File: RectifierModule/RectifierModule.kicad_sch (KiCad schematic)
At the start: 18 parts, among them J1 TransformerIn, J2 Rectified Out, J3 AuxIn, J4 VA, J5 Extra, J5 FAN, P1 Conn_WallPlug, U1 LM7812_TO220

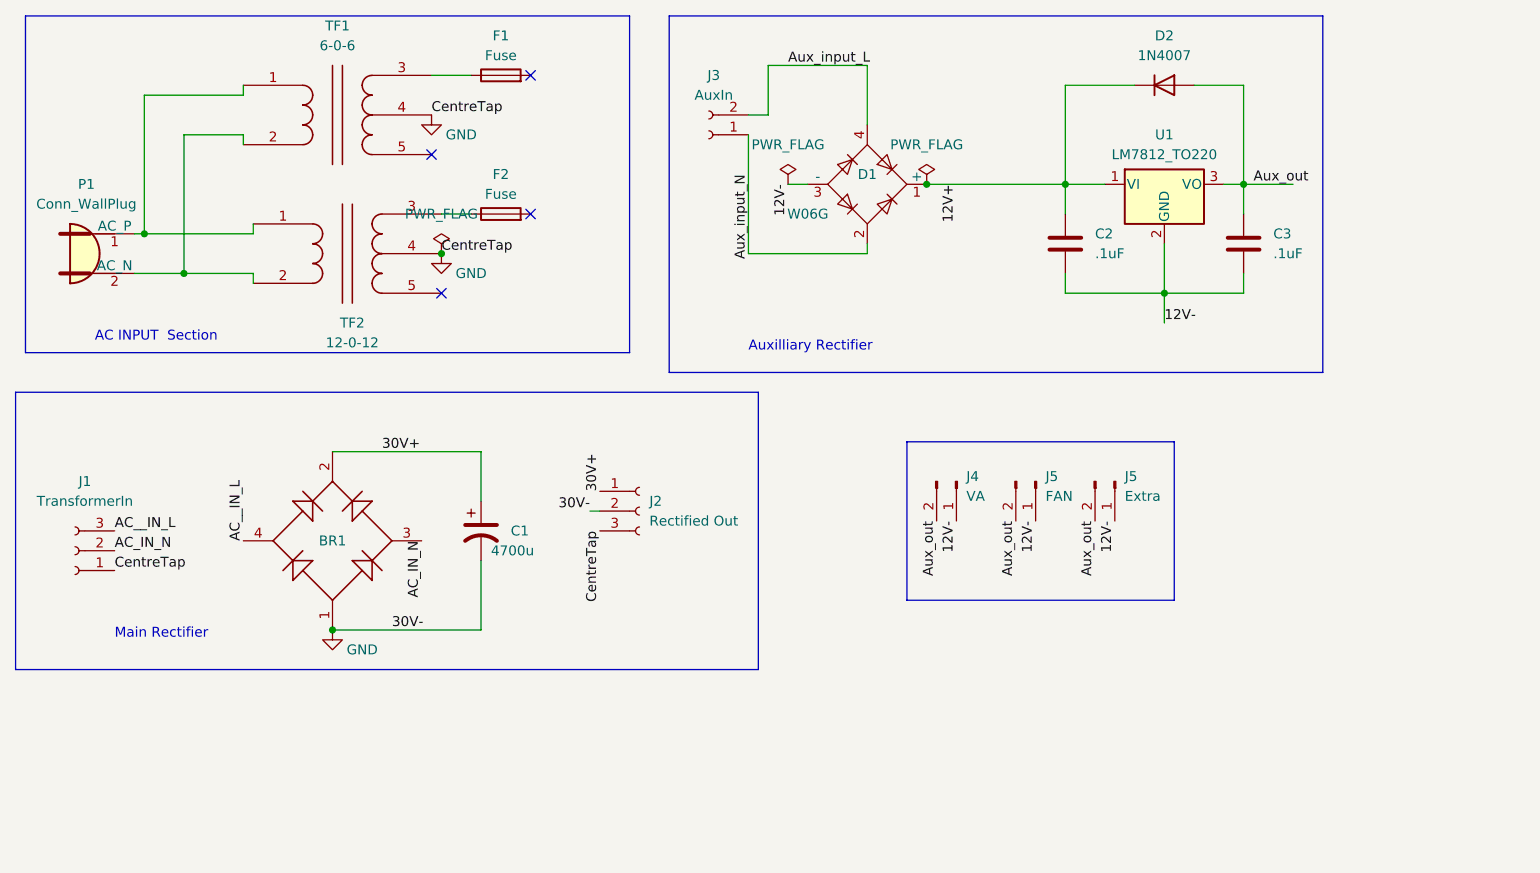
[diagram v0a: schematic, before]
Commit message: Updated net lists in the schematic
The schematic has all nets assigned to a net class. And the schematic has been tidied up
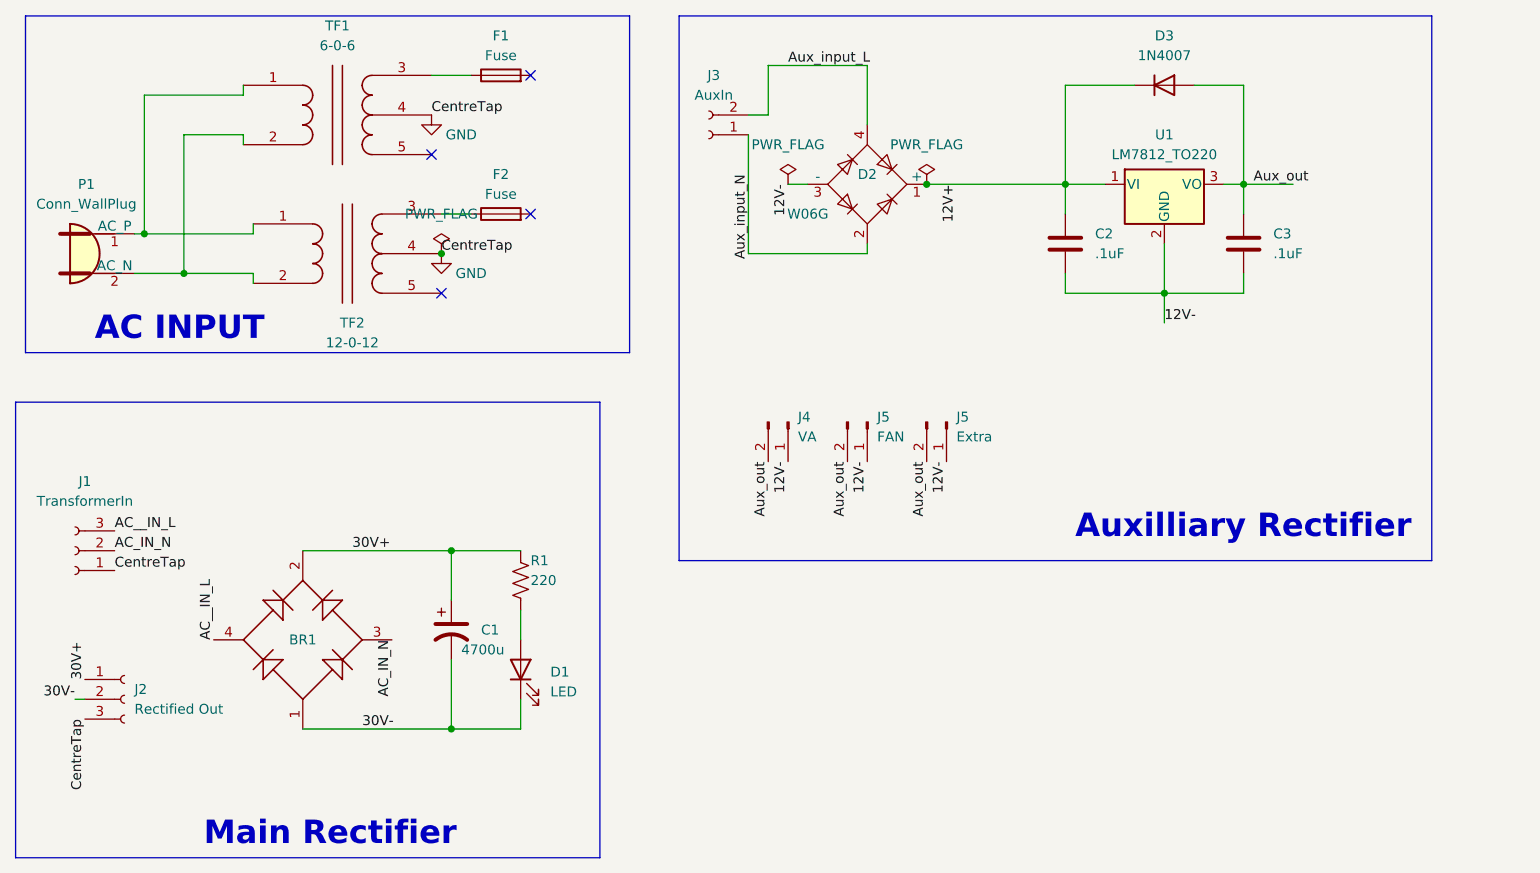
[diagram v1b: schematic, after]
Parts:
- added D1: LED, symbol Device:LED
- added R1: 220, symbol Device:R_US
- renumbered D1 to D2, D2 to D3
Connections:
- net 30V+: now also R1.1
- net GND: no longer BR1.1, C1.2, J2.2 (Pin_2)
- new net: D1.2 (A), R1.2
- new net 30V-: BR1.1, C1.2, D1.1 (K), J2.2 (Pin_2)
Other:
- note added: "AC INPUT"
- note removed: "AC INPUT Section"
- moved on the sheet: BR1, C1, J2, J4, J5

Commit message: Fixed all ERC warnings
There were several ERC warning regarding mismatch in port types. These have been fixed by modifying the library symbols
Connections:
- net AC__IN_L renamed AC_IN_L
- net GND renamed CentreTap
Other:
- moved on the sheet: F1, F2, TF1, TF2

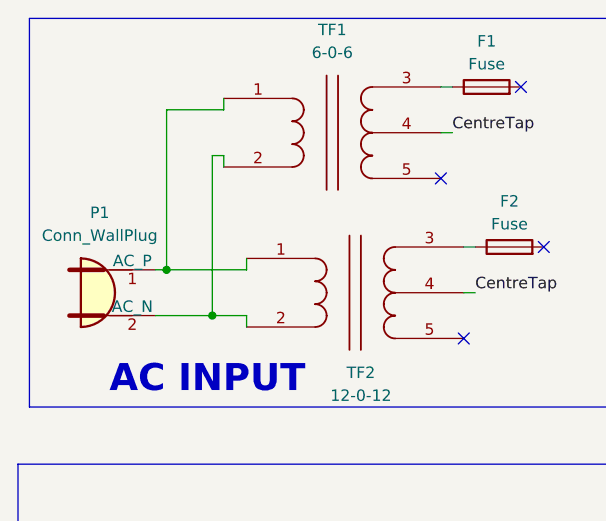
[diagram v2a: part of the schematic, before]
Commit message: Updated footprints
Updated foot prints of all the components in the list
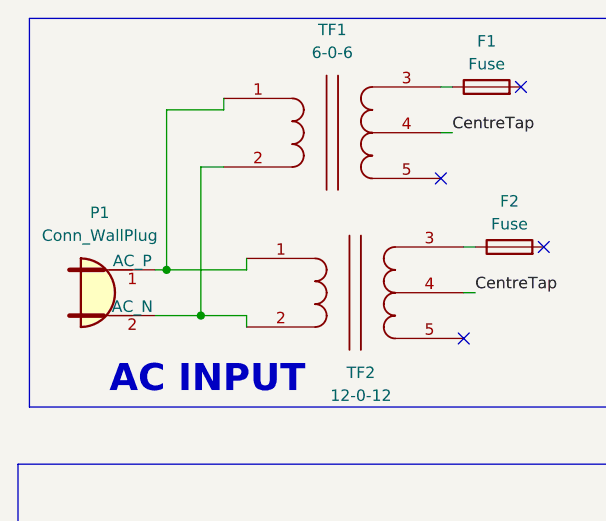
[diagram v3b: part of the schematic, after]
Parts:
- BR1: footprint package name for PCB layout -> BridgeRectifiers:BR-10X
- C1: footprint (none) -> Capacitor_THT:CP_Radial_D17.0mm_P7.50mm
- D1, J3: footprint (none) -> Connector_PinSocket_2.54mm:PinSocket_1x02_P2.54mm_Vertical
- J1, J2: footprint (none) -> Connector_JST:JST_VH_B3P-VH-B_1x03_P3.96mm_Vertical
- R1: footprint (none) -> Resistor_THT:R_Axial_DIN0207_L6.3mm_D2.5mm_P10.16mm_Horizontal
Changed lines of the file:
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@@
   (junction (at 30.48 43.18) (diameter 0) (color 0 0 0 0)
   )
-  (junction (at 35.56 48.26) (diameter 0) (color 0 0 0 0)
+  (junction (at 34.29 48.26) (diameter 0) (color 0 0 0 0)
   )
   (junction (at 69.85 83.82) (diameter 0) (color 0 0 0 0)
@@
     (stroke (width 0) (type default))
   )
-  (wire (pts (xy 29.21 48.26) (xy 35.56 48.26))
+  (wire (pts (xy 29.21 48.26) (xy 34.29 48.26))
     (stroke (width 0) (type default))
   )
@@
     (stroke (width 0) (type default))
   )
-  (wire (pts (xy 36.83 30.48) (xy 36.83 31.75))
-    (stroke (width 0) (type default))
-  )
   (wire (pts (xy 171.45 36.83) (xy 177.8 36.83))
     (stroke (width 0) (type default))
@@
     (stroke (width 0) (type default))
   )
-  (wire (pts (xy 35.56 30.48) (xy 36.83 30.48))
-    (stroke (width 0) (type default))
-  )
-  (wire (pts (xy 35.56 30.48) (xy 35.56 48.26))
+  (wire (pts (xy 34.29 31.75) (xy 36.83 31.75))
+    (stroke (width 0) (type default))
+  )
+  (wire (pts (xy 34.29 31.75) (xy 34.29 48.26))
     (stroke (width 0) (type default))
   )
@@
     (stroke (width 0) (type default))
   )
-  (wire (pts (xy 35.56 48.26) (xy 39.37 48.26))
+  (wire (pts (xy 34.29 48.26) (xy 39.37 48.26))
     (stroke (width 0) (type default))
   )
@@
   )
   (symbol (lib_name "TRANSFORMER_1") (lib_id "V_Passive:TRANSFORMER") (at 49.53 27.94 0) (unit 1)
-    (in_bom yes) (on_board yes) (dnp no) (fields_autoplaced)
+    (in_bom yes) (on_board no) (dnp no) (fields_autoplaced)
     (property "Reference" "TF1" (at 48.895 16.51 0)
       (effects (font (size 1.27 1.27)))
@@
       (effects (font (size 1.27 1.27)) hide)
     )
-    (property "Footprint" "package name for PCB layout" (at 50.8 95.25 0)
+    (property "Footprint" "BridgeRectifiers:BR-10X" (at 50.8 95.25 0)
       (effects (font (size 1.27 1.27)) hide)
     )
@@
   (symbol (lib_id "power:PWR_FLAG") (at 130.81 36.83 0) (unit 1)
     (in_bom yes) (on_board yes) (dnp no) (fields_autoplaced)
-    (property "Reference" "#FLG03" (at 130.81 34.925 0)
+    (property "Reference" "#FLG02" (at 130.81 34.925 0)
       (effects (font (size 1.27 1.27)) hide)
     )
@@
       (project "RectifierModule"
         (path "/85225bbb-a12f-4483-ac90-767368bd8ae2"
-          (reference "#FLG03") (unit 1)
+          (reference "#FLG02") (unit 1)
         )
       )
@@
       (effects (font (size 1.27 1.27)))
     )
-    (property "Footprint" "" (at 21.59 83.82 0)
+    (property "Footprint" "Connector_JST:JST_VH_B3P-VH-B_1x03_P3.96mm_Vertical" (at 21.59 83.82 0)
       (effects (font (size 1.27 1.27)) hide)
     )
@@
       (effects (font (size 1.27 1.27)) (justify left))
     )
-    (property "Footprint" "" (at 27.94 102.87 0)
+    (property "Footprint" "Connector_JST:JST_VH_B3P-VH-B_1x03_P3.96mm_Vertical" (at 27.94 102.87 0)
       (effects (font (size 1.27 1.27)) hide)
     )
@@
   (symbol (lib_id "power:PWR_FLAG") (at 113.03 36.83 0) (unit 1)
     (in_bom yes) (on_board yes) (dnp no) (fields_autoplaced)
-    (property "Reference" "#FLG02" (at 113.03 34.925 0)
+    (property "Reference" "#FLG01" (at 113.03 34.925 0)
       (effects (font (size 1.27 1.27)) hide)
     )
@@
       (project "RectifierModule"
         (path "/85225bbb-a12f-4483-ac90-767368bd8ae2"
-          (reference "#FLG02") (unit 1)
+          (reference "#FLG01") (unit 1)
         )
       )
@@
       (effects (font (size 1.27 1.27)) (justify left))
     )
-    (property "Footprint" "" (at 69.85 93.98 0)
+    (property "Footprint" "Capacitor_THT:CP_Radial_D17.0mm_P7.50mm" (at 69.85 93.98 0)
       (effects (font (size 1.27 1.27)) hide)
     )
@@
   )
   (symbol (lib_id "V_Passive:TRANSFORMER") (at 52.07 45.72 0) (unit 1)
-    (in_bom yes) (on_board yes) (dnp no)
+    (in_bom yes) (on_board no) (dnp no)
     (property "Reference" "TF2" (at 52.07 54.61 0)
       (effects (font (size 1.27 1.27)))
@@
       (effects (font (size 1.27 1.27)))
     )
-    (property "Footprint" "" (at 102.87 30.48 0)
+    (property "Footprint" "Connector_PinSocket_2.54mm:PinSocket_1x02_P2.54mm_Vertical" (at 102.87 30.48 0)
       (effects (font (size 1.27 1.27)) hide)
     )
@@
       (effects (font (size 1.27 1.27)) (justify right))
     )
-    (property "Footprint" "" (at 78.74 99.06 0)
+    (property "Footprint" "Connector_PinSocket_2.54mm:PinSocket_1x02_P2.54mm_Vertical" (at 78.74 99.06 0)
       (effects (font (size 1.27 1.27)) hide)
     )
@@
       (effects (font (size 1.27 1.27)) (justify left))
     )
-    (property "Footprint" "" (at 79.756 87.884 90)
-      (effects (font (size 1.27 1.27)) hide)
-    )
+    (property "Footprint" "Resistor_THT:R_Axial_DIN0207_L6.3mm_D2.5mm_P10.16mm_Horizontal" (at 79.756 87.884 90)
+      (effects (font (size 1.27 1.27)) hide)
+    )

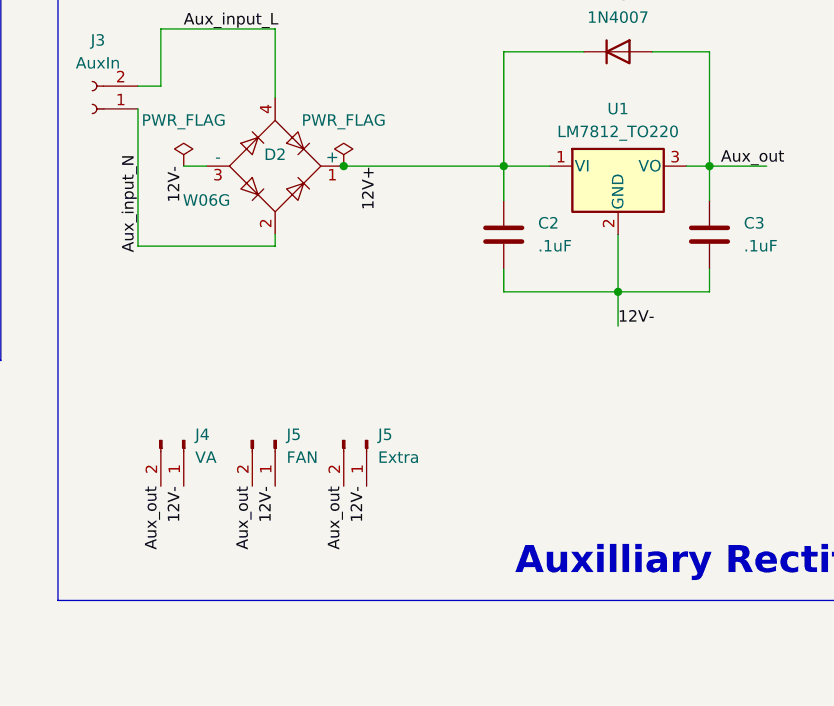
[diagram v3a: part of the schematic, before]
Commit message: Generated PCB layout
Some minor updates in the schematic and created the PCB layout for the rectifier module
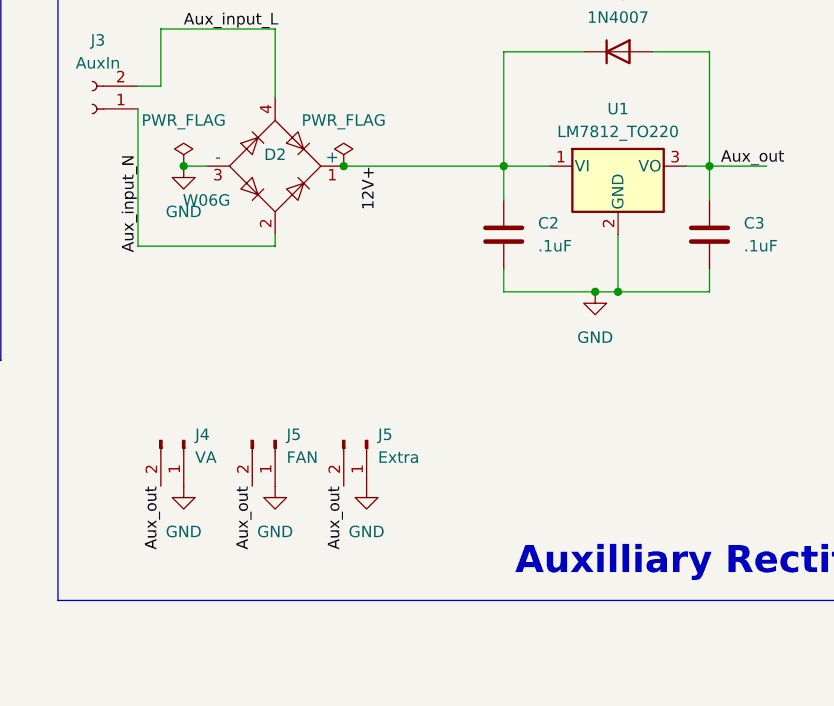
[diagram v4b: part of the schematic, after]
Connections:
- net 12V- renamed GND
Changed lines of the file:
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@@
     (rev "1")
+  )
+  (junction (at 113.03 36.83) (diameter 0) (color 0 0 0 0)
+  )
+  (junction (at 158.75 50.8) (diameter 0) (color 0 0 0 0)
   )
   (junction (at 30.48 43.18) (diameter 0) (color 0 0 0 0)
@@
     (stroke (width 0) (type default))
   )
-  (wire (pts (xy 148.59 50.8) (xy 161.29 50.8))
+  (wire (pts (xy 148.59 50.8) (xy 158.75 50.8))
     (stroke (width 0) (type default))
   )
@@
     (stroke (width 0) (type default))
   )
+  (wire (pts (xy 158.75 50.8) (xy 161.29 50.8))
+    (stroke (width 0) (type default))
+  )
   (wire (pts (xy 110.49 27.94) (xy 110.49 21.59))
     (stroke (width 0) (type default))
   )
   (wire (pts (xy 78.74 102.87) (xy 78.74 106.68))
-    (stroke (width 0) (type default))
-  )
-  (wire (pts (xy 161.29 50.8) (xy 161.29 54.61))
     (stroke (width 0) (type default))
   )
@@
     (effects (font (size 1.27 1.27)) (justify left bottom))
   )
-  (label "12V-" (at 123.19 72.39 270) (fields_autoplaced)
-    (effects (font (size 1.27 1.27)) (justify right bottom))
-  )
   (label "AC_IN_L" (at 39.37 95.25 90) (fields_autoplaced)
     (effects (font (size 1.27 1.27)) (justify left bottom))
@@
     (effects (font (size 1.27 1.27)) (justify right bottom))
   )
-  (label "12V-" (at 113.03 72.39 270) (fields_autoplaced)
-    (effects (font (size 1.27 1.27)) (justify right bottom))
-  )
-  (label "12V-" (at 161.29 54.61 0) (fields_autoplaced)
-    (effects (font (size 1.27 1.27)) (justify left bottom))
-  )
   (label "12V+" (at 134.62 36.83 270) (fields_autoplaced)
     (effects (font (size 1.27 1.27)) (justify right bottom))
@@
     (effects (font (size 1.27 1.27)) (justify right bottom))
   )
-  (label "12V-" (at 133.35 72.39 270) (fields_autoplaced)
-    (effects (font (size 1.27 1.27)) (justify right bottom))
-  )
   (label "30V-" (at 21.59 102.87 180) (fields_autoplaced)
     (effects (font (size 1.27 1.27)) (justify right bottom))
@@
   (label "30V-" (at 58.42 106.68 0) (fields_autoplaced)
     (effects (font (size 1.27 1.27)) (justify left bottom))
-  )
-  (label "12V-" (at 113.03 36.83 270) (fields_autoplaced)
-    (effects (font (size 1.27 1.27)) (justify right bottom))
   )
   (label "Aux_input_L" (at 113.03 21.59 0) (fields_autoplaced)
@@
     )
   )
+  (symbol (lib_id "power:GND") (at 123.19 72.39 0) (unit 1)
+    (in_bom yes) (on_board yes) (dnp no) (fields_autoplaced)
+    (property "Reference" "#PWR04" (at 123.19 78.74 0)
+      (effects (font (size 1.27 1.27)) hide)
+    )
+    (property "Value" "GND" (at 123.19 77.47 0)
+      (effects (font (size 1.27 1.27)))
+    )
+    (property "Footprint" "" (at 123.19 72.39 0)
+      (effects (font (size 1.27 1.27)) hide)
+    )
+    (property "Datasheet" "" (at 123.19 72.39 0)
+      (effects (font (size 1.27 1.27)) hide)
+    )
+    (pin "1")
+    (instances
+      (project "RectifierModule"
+        (path "/85225bbb-a12f-4483-ac90-767368bd8ae2"
+          (reference "#PWR04") (unit 1)
+        )
+      )
+    )
+  )
+  (symbol (lib_id "power:GND") (at 113.03 72.39 0) (unit 1)
+    (in_bom yes) (on_board yes) (dnp no) (fields_autoplaced)
+    (property "Reference" "#PWR03" (at 113.03 78.74 0)
+      (effects (font (size 1.27 1.27)) hide)
+    )
+    (property "Value" "GND" (at 113.03 77.47 0)
+      (effects (font (size 1.27 1.27)))
+    )
+    (property "Footprint" "" (at 113.03 72.39 0)
+      (effects (font (size 1.27 1.27)) hide)
+    )
+    (property "Datasheet" "" (at 113.03 72.39 0)
+      (effects (font (size 1.27 1.27)) hide)
+    )
+    (pin "1")
+    (instances
+      (project "RectifierModule"
+        (path "/85225bbb-a12f-4483-ac90-767368bd8ae2"
+          (reference "#PWR03") (unit 1)
+        )
+      )
+    )
+  )
   (symbol (lib_id "Connector:Conn_01x02_Pin") (at 123.19 67.31 270) (unit 1)
     (in_bom yes) (on_board yes) (dnp no) (fields_autoplaced)
@@
     )
   )
+  (symbol (lib_id "power:GND") (at 133.35 72.39 0) (unit 1)
+    (in_bom yes) (on_board yes) (dnp no) (fields_autoplaced)
+    (property "Reference" "#PWR05" (at 133.35 78.74 0)
+      (effects (font (size 1.27 1.27)) hide)
+    )
+    (property "Value" "GND" (at 133.35 77.47 0)
+      (effects (font (size 1.27 1.27)))
+    )
+    (property "Footprint" "" (at 133.35 72.39 0)
+      (effects (font (size 1.27 1.27)) hide)
+    )
+    (property "Datasheet" "" (at 133.35 72.39 0)
+      (effects (font (size 1.27 1.27)) hide)
+    )
+    (pin "1")
+    (instances
+      (project "RectifierModule"
+        (path "/85225bbb-a12f-4483-ac90-767368bd8ae2"
+          (reference "#PWR05") (unit 1)
+        )
+      )
+    )
+  )
   (symbol (lib_id "Device:C") (at 171.45 44.45 0) (unit 1)
     (in_bom yes) (on_board yes) (dnp no) (fields_autoplaced)
@@
     )
   )
+  (symbol (lib_id "power:GND") (at 113.03 36.83 0) (unit 1)
+    (in_bom yes) (on_board yes) (dnp no) (fields_autoplaced)
+    (property "Reference" "#PWR01" (at 113.03 43.18 0)
+      (effects (font (size 1.27 1.27)) hide)
+    )
+    (property "Value" "GND" (at 113.03 41.91 0)
+      (effects (font (size 1.27 1.27)))
+    )
+    (property "Footprint" "" (at 113.03 36.83 0)
+      (effects (font (size 1.27 1.27)) hide)
+    )
+    (property "Datasheet" "" (at 113.03 36.83 0)
+      (effects (font (size 1.27 1.27)) hide)
+    )
+    (pin "1")
+    (instances
+      (project "RectifierModule"
+        (path "/85225bbb-a12f-4483-ac90-767368bd8ae2"
+          (reference "#PWR01") (unit 1)
+        )
+      )
+    )
+  )
   (symbol (lib_id "V_Passive:TRANSFORMER") (at 52.07 45.72 0) (unit 1)
     (in_bom yes) (on_board no) (dnp no)
@@
         )
       )
+    )
+  )
+  (symbol (lib_id "power:GND") (at 158.75 50.8 0) (unit 1)
+    (in_bom yes) (on_board yes) (dnp no) (fields_autoplaced)
+    (property "Reference" "#PWR02" (at 158.75 57.15 0)
+      (effects (font (size 1.27 1.27)) hide)
+    )
+    (property "Value" "GND" (at 158.75 55.88 0)
+      (effects (font (size 1.27 1.27)))
+    )
+    (property "Footprint" "" (at 158.75 50.8 0)
+      (effects (font (size 1.27 1.27)) hide)
+    )
+    (property "Datasheet" "" (at 158.75 50.8 0)
+      (effects (font (size 1.27 1.27)) hide)
+    )
+    (pin "1")
+    (instances
+      (project "RectifierModule"
+        (path "/85225bbb-a12f-4483-ac90-767368bd8ae2"
+          (reference "#PWR02") (unit 1)
+        )
+      )
